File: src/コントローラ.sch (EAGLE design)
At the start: 8 parts

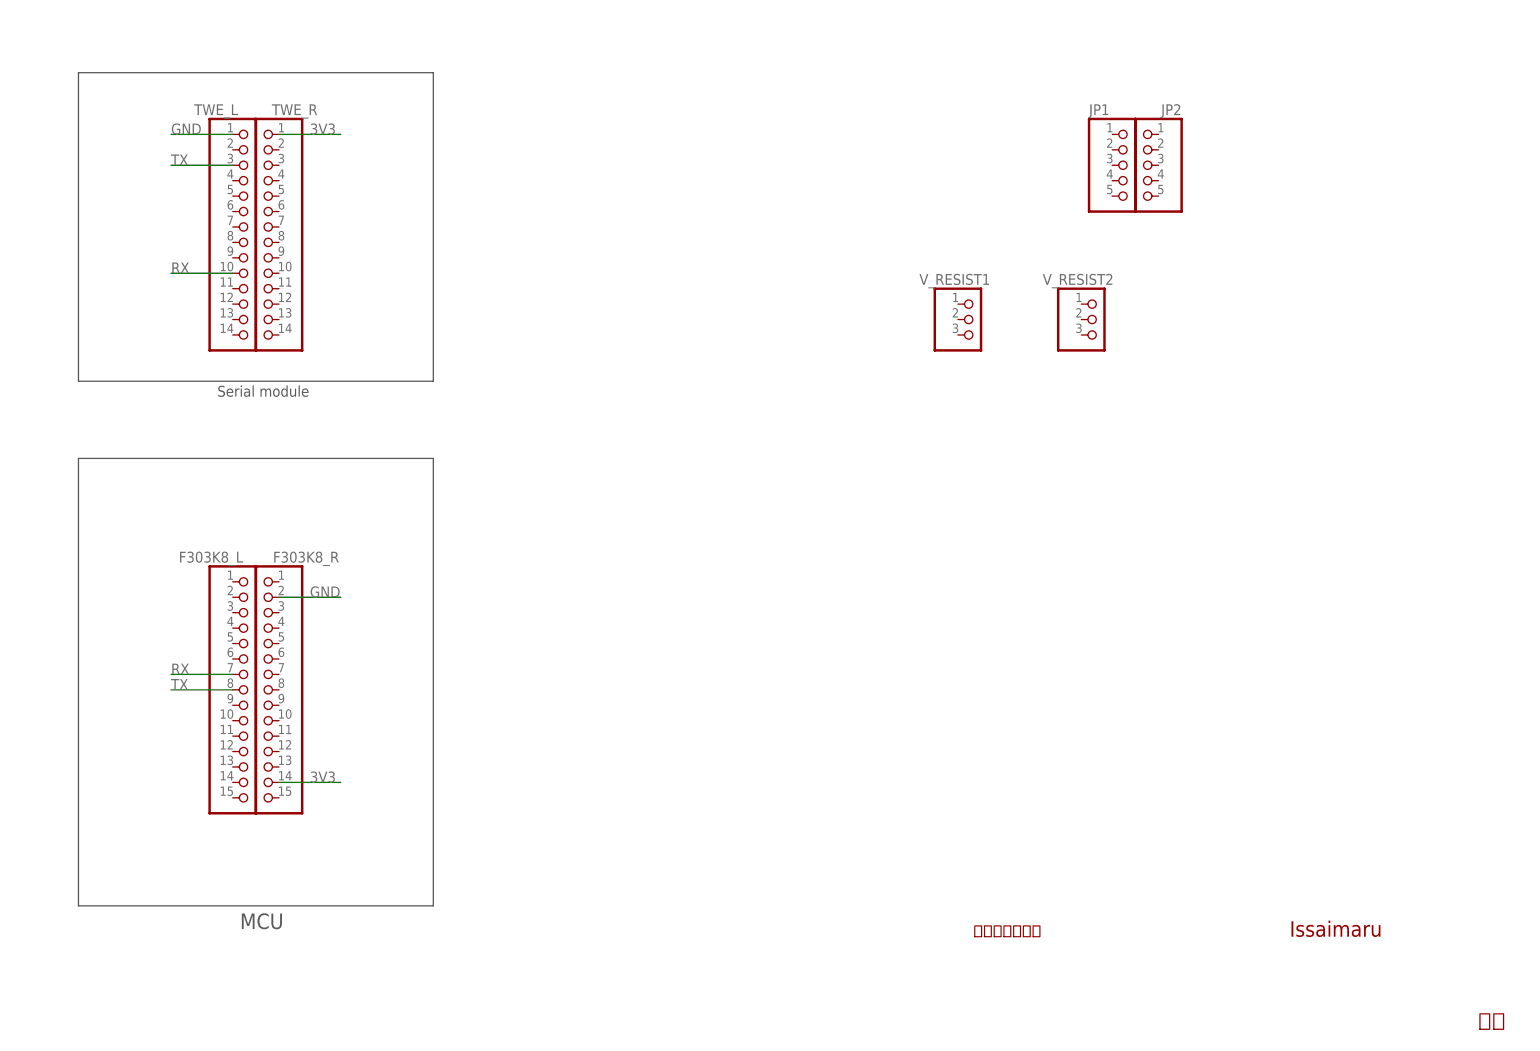
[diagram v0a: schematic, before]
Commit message: [add]コントローラに対する進捗dxを生成✅
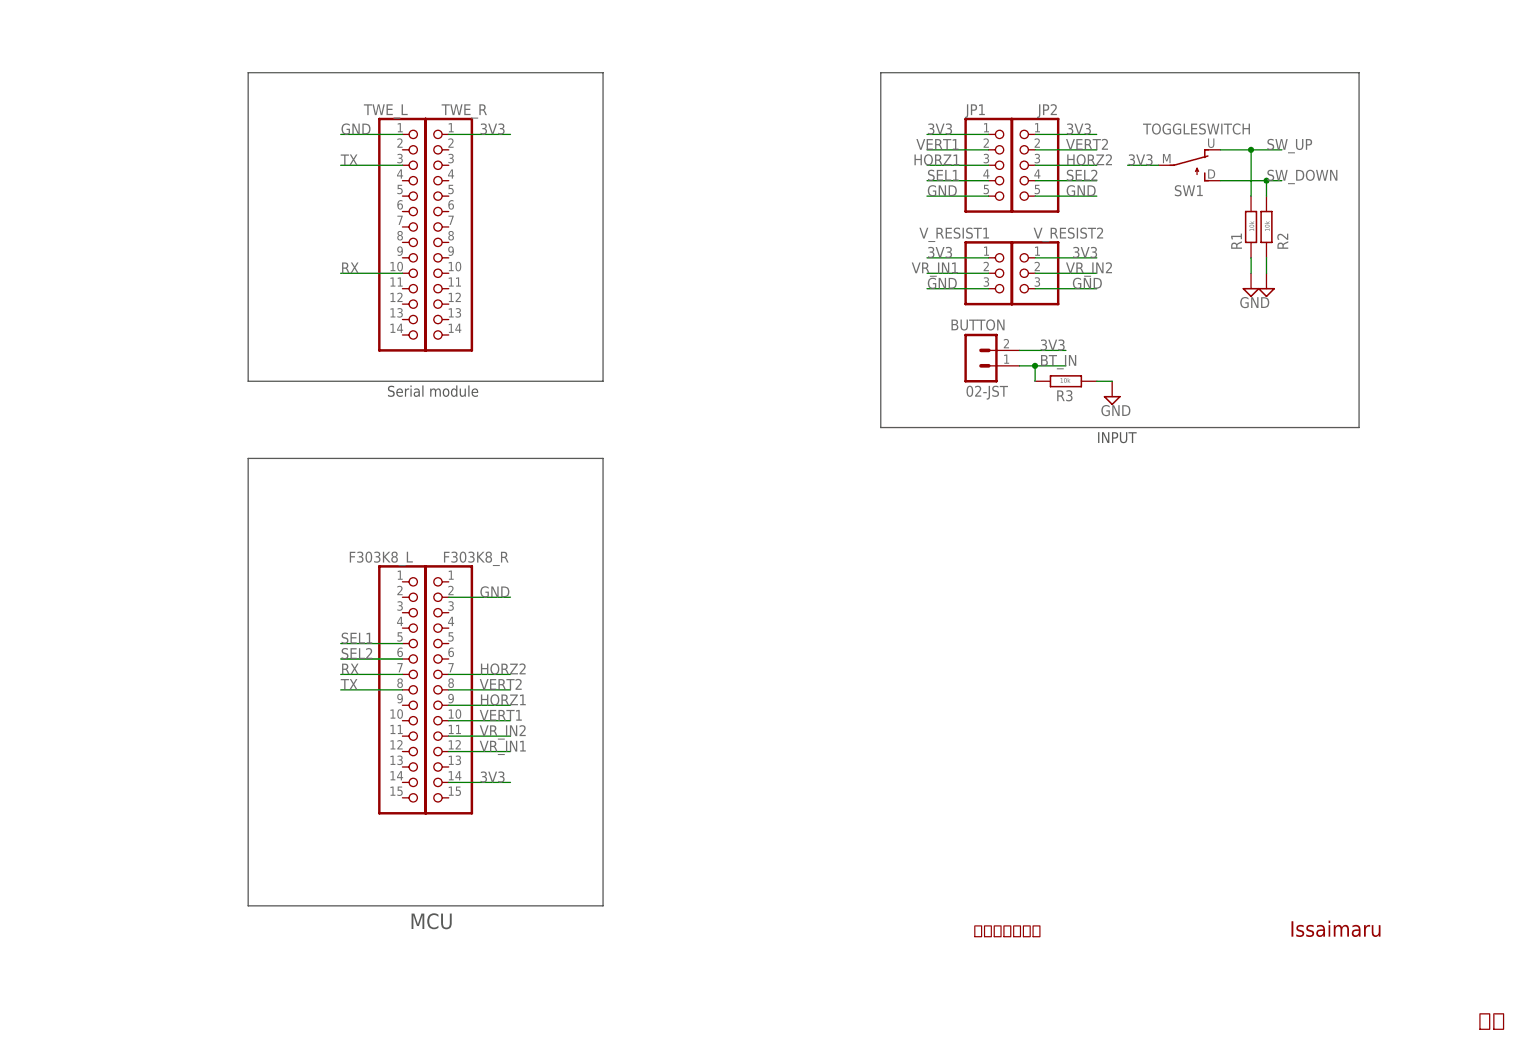
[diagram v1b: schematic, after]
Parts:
- added BUTTON: 02-JST, con-jst-xh:02-JST
- added R1, R2, R3: 10k, rcl:R-EU_0204/7
- added SW1: TOGGLESWITCH, ToggleSwitch:TOGGLESWITCH
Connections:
- new net BT_IN: BUTTON.1, R3.2
- new net HORZ1: F303K8_R.9, JP1.3
- new net HORZ2: F303K8_R.7, JP2.3
- new net SEL1: F303K8_L.5, JP1.4
- new net SEL2: F303K8_L.6, JP2.4
- new net SW_DOWN: R2.2, SW1.R
- new net SW_UP: R1.2, SW1.L
- new net VERT1: F303K8_R.10, JP1.2
- new net VERT2: F303K8_R.8, JP2.2
- new net VR_IN1: F303K8_R.12, V_RESIST1.2
- new net VR_IN2: F303K8_R.11, V_RESIST2.2
- net 3V3: now also BUTTON.2, JP1.1, JP2.1, SW1.C, V_RESIST1.1, V_RESIST2.1
- net GND: now also JP1.5, JP2.5, R1.1, R2.1, R3.1, V_RESIST1.3, V_RESIST2.3
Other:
- note added: "INPUT"
- moved on the sheet: F303K8_L, F303K8_R, JP1, JP2, TWE_L, TWE_R, V_RESIST1, V_RESIST2

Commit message: [add]コントローラー.brdの追加
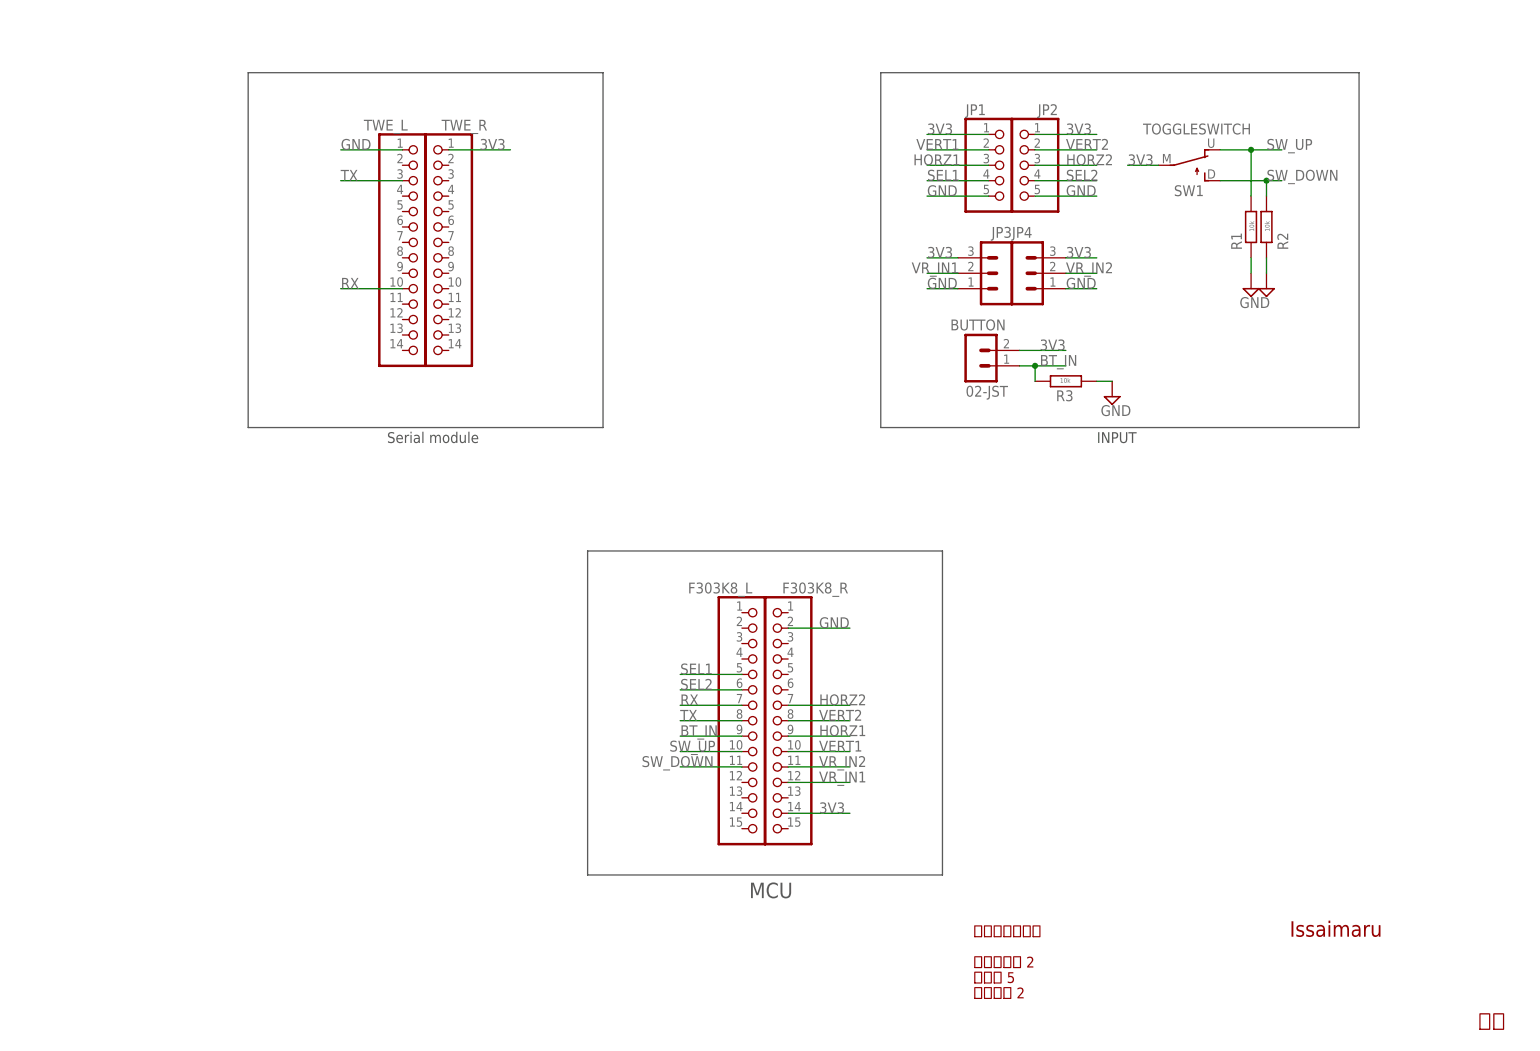
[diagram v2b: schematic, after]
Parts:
- removed V_RESIST1, V_RESIST2: (no value), pinhead:PINHD-1X3
- added JP3, JP4: (no value), con-jst-xh:03-JST
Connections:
- net 3V3: now also JP3.3, JP4.3; no longer V_RESIST1.1, V_RESIST2.1
- net BT_IN: now also F303K8_L.9
- net GND: now also JP3.1, JP4.1; no longer V_RESIST1.3, V_RESIST2.3
- net SW_DOWN: now also F303K8_L.11
- net SW_UP: now also F303K8_L.10
- net VR_IN1: now also JP3.2; no longer V_RESIST1.2
- net VR_IN2: now also JP4.2; no longer V_RESIST2.2
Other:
- note added: "スティック 2"
- note added: "ボタン 5"
- note added: "可変抵抗 2"
- moved on the sheet: F303K8_L, F303K8_R, TWE_L, TWE_R

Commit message: fix
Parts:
- added BUTTON2: 02-JST, con-jst-xh:02-JST
- added KAHEN: (no value), pinhead:PINHD-1X3
- added R4, R5, R6: 10k, rcl:R-EU_0204/7
- added R7, R8, R9: (no value), rcl:R-EU_0207/7
- added SLIDESWITCH: SLEDESWITCH, slide switch:SLEDESWITCH
- added SW2: TOGGLESWITCH, ToggleSwitch:TOGGLESWITCH
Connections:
- net SW_DOWN renamed SW_DOWN1
- net SW_UP renamed SW_UP1
- removed net BT_IN: BUTTON.1, F303K8_L.9, R3.2
- new net BT_IN1: BUTTON.1, F303K8_L.9, R5.2
- new net BT_IN2: F303K8_L.14, R6.2
- new net CONNECT: SLIDESWITCH.1
- new net CONNECT1: SLIDESWITCH.2
- new net N$1: R7.2, SLIDESWITCH.5
- new net N$2: R8.2, SLIDESWITCH.6
- new net N$5: KAHEN.2
- new net N$7: R9.1
- new net RT_IN2: BUTTON2.1
- new net SW_DOWN2: F303K8_L.13, R4.2, SW2.R
- new net SW_UP2: F303K8_L.12, R3.2, SW2.L
- new net SYUUDOUSI＋: R9.2
- net 3V3: now also BUTTON2.2, KAHEN.3, SLIDESWITCH.3, SLIDESWITCH.4, SW2.C
- net GND: now also KAHEN.1, R4.1, R5.1, R6.1, R7.1, R8.1
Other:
- note added: "GND"
- moved on the sheet: BUTTON, F303K8_L, F303K8_R, JP1, JP2, JP3, JP4, R1, R2, R3, SW1, TWE_L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

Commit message: fix
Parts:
- removed JP3, JP4: (no value), con-jst-xh:03-JST
- removed R9: (no value), rcl:R-EU_0207/7
- removed SLIDESWITCH: SLEDESWITCH, slide switch:SLEDESWITCH
- removed SW1, SW2: TOGGLESWITCH, ToggleSwitch:TOGGLESWITCH
- added C1, C2: (no value), rcl:C-EU025-024X044
- added EMAERGENCY: 02-JST, con-jst-xh:02-JST
- added JP10, JP11, JP12, JP13, JP14, JP9: (no value), pinhead:PINHD-1X2
- added JP8, TOGLLESWITCH: (no value), con-jst-xh (1):03-JST
- added LED2, LED3, LED4, LED5, LED7: (no value), led:LED5MM
- added R10: 10k, rcl:R-EU_0204/7
- JP1, JP2: device pinhead:PINHD-1X5 -> pinhead:PINHD-1X2
- R7, R8: value (none) -> 10k; device rcl:R-EU_0207/7 -> rcl:R-EU_0204/7
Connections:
- removed net CONNECT: SLIDESWITCH.1
- removed net CONNECT1: SLIDESWITCH.2
- removed net HORZ1: F303K8_R.9, JP1.3
- removed net HORZ2: F303K8_R.7, JP2.3
- removed net N$2: R8.2, SLIDESWITCH.6
- removed net RT_IN2: BUTTON2.1
- removed net SW_DOWN1: F303K8_L.11, R2.2, SW1.R
- removed net SW_DOWN2: F303K8_L.13, R4.2, SW2.R
- removed net SW_UP1: F303K8_L.10, R1.2, SW1.L
- removed net SW_UP2: F303K8_L.12, R3.2, SW2.L
- removed net SYUUDOUSI＋: R9.2
- removed net VERT1: F303K8_R.10, JP1.2
- removed net VERT2: F303K8_R.8, JP2.2
- removed net VR_IN1: F303K8_R.12, JP3.2
- removed net VR_IN2: F303K8_R.11, JP4.2
- new net AIN5: F303K8_R.6, JP8.2, KAHEN.2, R5.2
- new net L/R1: F303K8_R.10, JP9.2
- new net L/R2: F303K8_R.8, JP11.2
- new net N$3: LED4.A, R8.1
- new net N$4: LED3.A, R7.1
- new net NRST: EMAERGENCY.2, F303K8_R.3
- new net SW\_UP: R3.2, R7.2, TOGLLESWITCH.3
- new net SW_DOWN: F303K8_L.11, R4.2, R6.2, TOGLLESWITCH.1
- new net SW_UP: F303K8_L.10
- new net U/D1: F303K8_R.9, JP1.1
- new net U/D2: F303K8_R.7, JP12.1
- net 3V3: now also C1.1, C2.1, JP11.1, JP8.3, JP9.1, KAHEN.1, TOGLLESWITCH.2; no longer JP1.1, JP2.1, JP3.3, JP4.3, KAHEN.3, SLIDESWITCH.3, SLIDESWITCH.4, SW1.C, SW2.C
- net BT_IN1: now also R1.2, R8.2; no longer R5.2
- net BT_IN2: now also BUTTON2.1, R10.2, R2.2; no longer R6.2
- net GND: now also C1.2, C2.2, EMAERGENCY.1, JP1.2, JP12.2, JP8.1, KAHEN.3, LED2.C, LED3.C, LED4.C, LED5.C, LED7.C; no longer JP1.5, JP2.5, JP3.1, JP4.1, KAHEN.1, R5.1, R6.1, R7.1, R8.1
- net N$1: now also LED7.A, R5.1; no longer R7.2, SLIDESWITCH.5
- net N$5: now also LED2.A, R6.1; no longer KAHEN.2
- net N$7: now also LED5.A, R10.1; no longer R9.1
- net SEL1: no longer JP1.4
- net SEL2: no longer JP2.4
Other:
- note added: "Analogstick"
- note added: "Button"
- note added: "TOGGLESWITCH"
- note removed: "INPUT"
- moved on the sheet: BUTTON, BUTTON2, KAHEN, R1, R2, R3, R4, R5, R6, R7, R8

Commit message: [add]コントローラAoi
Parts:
- removed LED7: (no value), led:LED5MM
- removed R10: 10k, rcl:R-EU_0204/7
- added LED1, LED6: 02-JST, con-jst-xh (1):02-JST
- added R11, R9: 100, rcl:R-EU_0204/7
- LED2, LED3, LED4, LED5: value (none) -> 02-JST; device led:LED5MM -> con-jst-xh (1):02-JST
- R5, R6, R7, R8: value 10k -> 100
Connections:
- removed net N$3: LED4.A, R8.1
- removed net N$4: LED3.A, R7.1
- removed net N$5: LED2.A, R6.1
- removed net N$7: LED5.A, R10.1
- new net D1: F303K8_L.12, LED1.2, R5.1, TWE_R.14
- net AIN5: now also LED6.2, R9.1; no longer R5.2
- net BT_IN1: now also LED2.2, R11.1; no longer R8.2
- net BT_IN2: now also LED3.2, R6.1; no longer R10.2
- net GND: now also LED1.1, LED2.1, LED3.1, LED4.1, LED5.1, LED6.1, R11.2, R5.2, R6.2, R7.2, R8.2, R9.2; no longer C1.2, JP1.2, LED2.C, LED3.C, LED4.C, LED5.C, LED7.C
- net N$1: now also C1.2, JP1.2; no longer LED7.A, R5.1
- net SW\_UP: no longer R7.2
- net SW_DOWN: now also LED5.2, R8.1; no longer R6.2
- net SW_UP: now also LED4.2, R7.1
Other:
- note removed: "GND"
- moved on the sheet: BUTTON, EMAERGENCY, R1, R3, R4, R5, R6, R7, R8

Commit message: [add]コントローラ　Aoi
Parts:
- removed R11: 100, rcl:R-EU_0204/7
- removed TOGLLESWITCH: (no value), con-jst-xh (1):03-JST
- added PIN, PINSOCKET: (no value), pinhead:PINHD-1X15
- added R10: 100, rcl:R-EU_0204/7
- added TOGGLESWITCH: (no value), con-jst-xh (1):03-JST
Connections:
- removed net SW\_UP: R3.2, TOGLLESWITCH.3
- new net N$8: PINSOCKET.3
- net 3V3: now also PIN.15, PINSOCKET.15, TOGGLESWITCH.2; no longer TOGLLESWITCH.2
- net AIN5: now also PIN.14, PINSOCKET.14, R10.1; no longer R9.1
- net BT_IN1: now also PIN.7, PINSOCKET.7, R6.1; no longer R11.1
- net BT_IN2: now also F303K8_L.10, PIN.6, PINSOCKET.6, R7.1; no longer F303K8_L.14, R6.1
- net D1: now also F303K8_L.14; no longer F303K8_L.12
- net GND: now also C1.2, JP1.2, PIN.13, PINSOCKET.13, R10.2; no longer R11.2
- net N$1: now also PIN.3; no longer C1.2, JP1.2
- net SW_DOWN: now also F303K8_L.12, PIN.4, PINSOCKET.4, R9.1, TOGGLESWITCH.3; no longer F303K8_L.11, R8.1, TOGLLESWITCH.1
- net SW_UP: now also F303K8_L.11, PIN.5, PINSOCKET.5, R3.2, R8.1, TOGGLESWITCH.1; no longer F303K8_L.10, R7.1
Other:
- note removed: "TOGGLESWITCH"
- moved on the sheet: BUTTON, BUTTON2, C1, C2, EMAERGENCY, F303K8_L, F303K8_R, JP1, JP10, JP11, JP12, JP13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

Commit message: [add]コントローラ　Aoi
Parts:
- removed JP8: (no value), con-jst-xh (1):03-JST
- KAHEN: device pinhead:PINHD-1X3 -> con-jst-xh (1):03-JST
- PIN, PINSOCKET: device pinhead:PINHD-1X15 -> pinhead:PINHD-1X7
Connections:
- removed net AIN5: F303K8_R.6, JP8.2, KAHEN.2, LED6.2, PIN.14, PINSOCKET.14, R10.1
- removed net D1: F303K8_L.14, LED1.2, R5.1, TWE_R.14
- removed net N$1: PIN.3
- removed net N$8: PINSOCKET.3
- removed net SEL1: F303K8_L.5
- removed net SEL2: F303K8_L.6
- new net KN: F303K8_L.11, KAHEN.2, LED6.2, PIN.1, PINSOCKET.1
- new net N$10: LED5.1, R9.1
- new net N$11: LED4.1, R8.1
- new net N$4: LED1.1, R5.1
- new net N$5: LED2.1, R6.1
- new net N$7: LED3.1, R7.1
- new net N$9: LED6.1, R10.1
- new net TW: F303K8_L.13, LED1.2
- net 3V3: now also KAHEN.3, PIN.7, PINSOCKET.7; no longer JP8.3, KAHEN.1, PIN.15, PINSOCKET.15
- net BT_IN1: now also F303K8_L.5, PIN.5, PINSOCKET.5; no longer F303K8_L.9, PIN.7, PINSOCKET.7, R6.1
- net BT_IN2: now also F303K8_L.6, PIN.4, PINSOCKET.4; no longer F303K8_L.10, PIN.6, PINSOCKET.6, R7.1
- net GND: now also KAHEN.1, PIN.6, PINSOCKET.6; no longer JP8.1, KAHEN.3, LED1.1, LED2.1, LED3.1, LED4.1, LED5.1, LED6.1, PIN.13, PINSOCKET.13
- net SW_DOWN: now also F303K8_L.10, PIN.2, PINSOCKET.2; no longer F303K8_L.12, PIN.4, PINSOCKET.4, R9.1
- net SW_UP: now also F303K8_L.9, PIN.3, PINSOCKET.3; no longer F303K8_L.11, PIN.5, PINSOCKET.5, R8.1
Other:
- note added: "KAHEN"
- moved on the sheet: EMAERGENCY, R10, R3, R4, R5, R6, R7, R8, R9, TOGGLESWITCH
